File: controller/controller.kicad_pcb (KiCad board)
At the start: 2 copper layers, 58.4 x 38.1 mm, 6 parts, among them J1 Input, J2 Control, J3 Pump, J4 Fan, K1 Auto

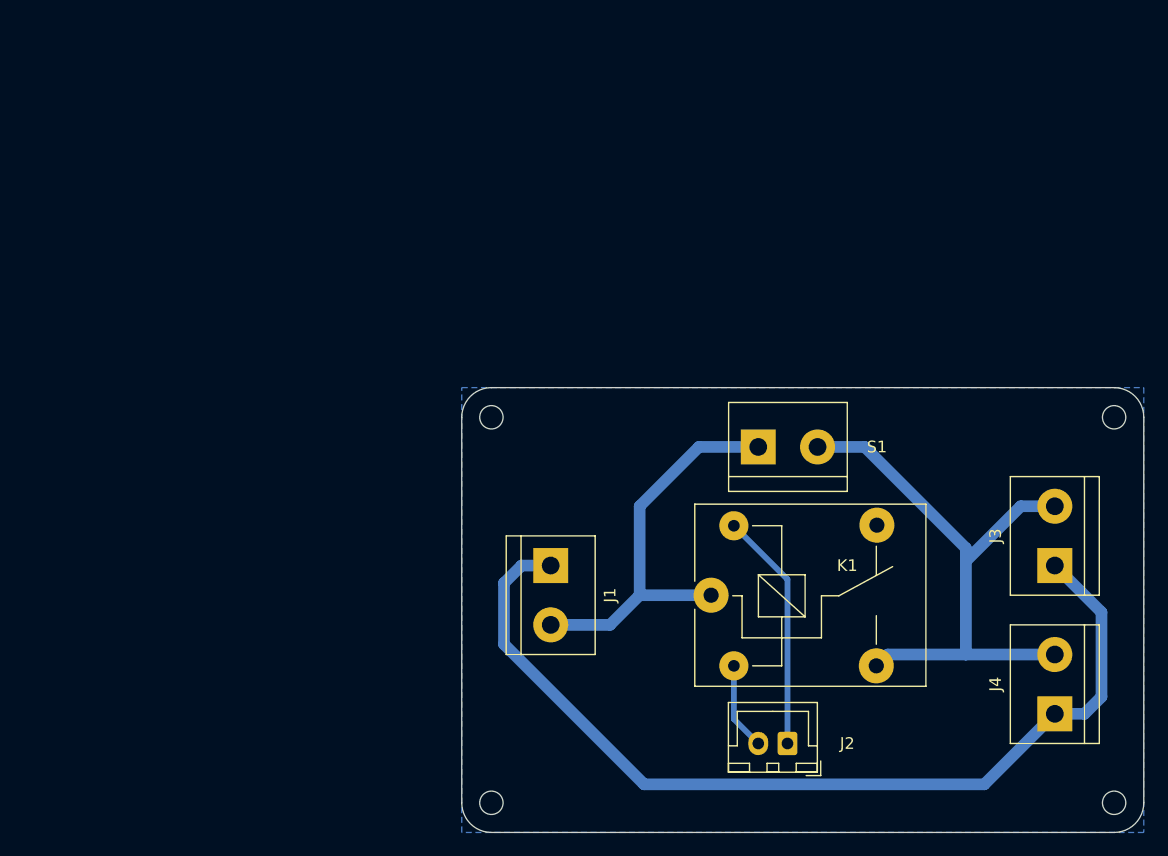
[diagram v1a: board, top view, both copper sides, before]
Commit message: Controller rev. 2 (single output)
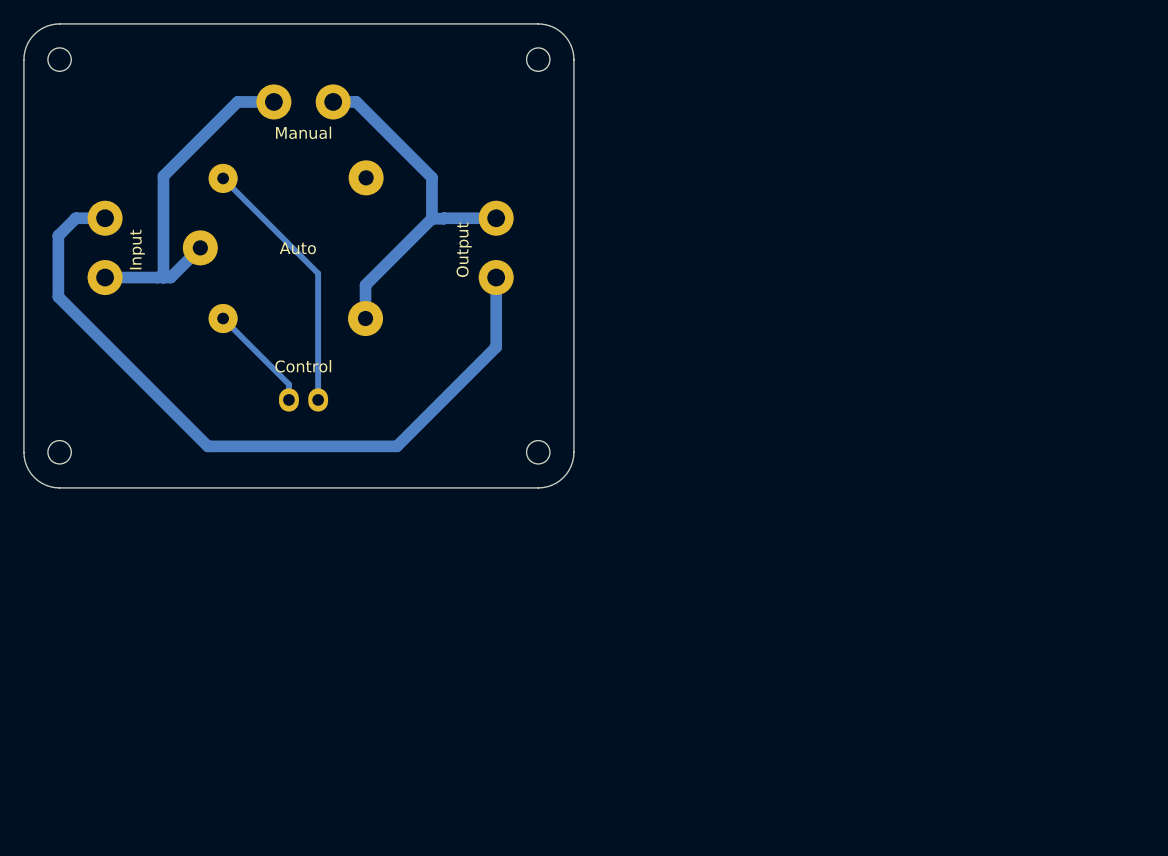
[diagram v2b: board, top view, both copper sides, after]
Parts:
- removed J4: Fan, TerminalBlock:TerminalBlock_bornier-2_P5.08mm
- J3: value Pump -> Output
- moved J3 53.8 mm to (117.2, 71.8)
- moved K1 52.9 mm to (91.9, 69.3)
- moved S1 50.9 mm to (98.2, 56.8)
- moved J2 49.8 mm to (102.0, 82.3)
- moved J1 48.4 mm to (83.8, 66.8)
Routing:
- net Net-(J3-Pin_2): track 51.7 -> 31.1 mm
- net Net-(J1-Pin_1): track 82.0 -> 62.1 mm
- net Net-(J1-Pin_2): track 34.7 -> 30.0 mm
- net Net-(J2-Pin_2): track 7.52 -> 9.31 mm
- net Net-(J2-Pin_1): track 20.6 -> 22.3 mm
- removed copper zone on B.Cu, net (none)
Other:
- board size 58.4 x 38.1 mm -> 47.1 x 39.7 mm
